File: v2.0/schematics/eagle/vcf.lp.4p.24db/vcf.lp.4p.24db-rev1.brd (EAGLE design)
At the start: 98.7 x 54.6 mm, 97 parts, among them IC1 TL082P, IC2 TL084P, IC3 LM13700N, IC4 LM13700N, IC5 LM13700N, IC6 TL082P, IC7 TL082P, IC8 TL082P, J1 IN, J2 OUT, T1 2N3904, T2 2N3904, T3 2N3904, T4 2N3906, T5 2N3906, T6 2N3906, T7 2N3906

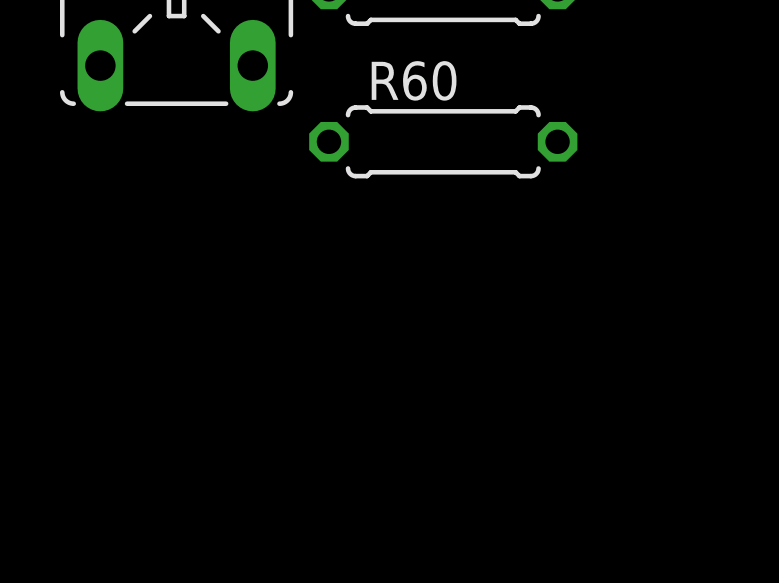
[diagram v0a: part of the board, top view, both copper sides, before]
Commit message: VFC-LP: Upates from schem review
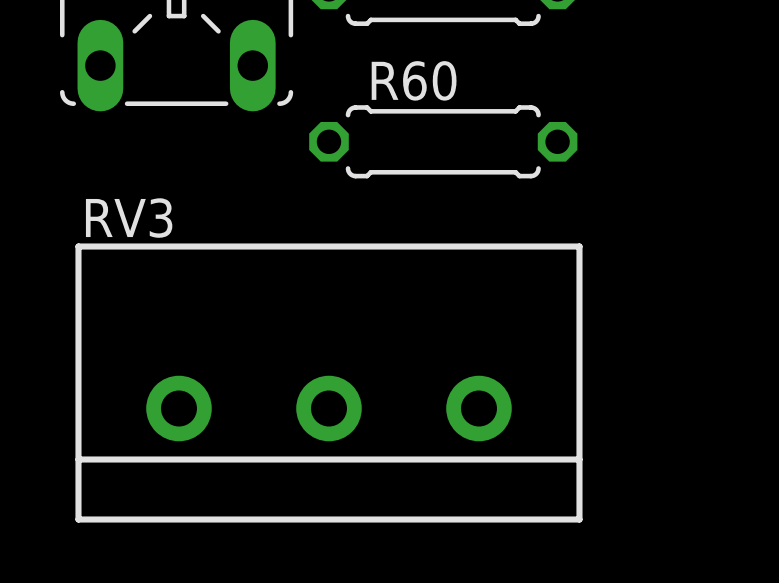
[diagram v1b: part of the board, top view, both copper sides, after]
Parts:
- added RV3: 100K (B), _common:_COMMON_3RP/1610N
- R27, R33: value 39K -> 43K
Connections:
- removed net N$54: R55.E, R57.1
- new net N$62: J1.P$3, RV3.2
- new net N$64: R55.E, R57.1, RV1.2
- net +12V: no longer RV1.2
- net 0V: now also RV3.1
- net N$49: now also RV3.3; no longer J1.P$3
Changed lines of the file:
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@@
 <attribute name="VALUE" x="-51.816" y="-178.3588" size="1.27" layer="27" ratio="10"/>
 </element>
-<element name="R27" library="resistor" package="0207/7" value="39K" x="-49.53" y="-182.88" smashed="yes">
+<element name="R27" library="resistor" package="0207/7" value="43K" x="-49.53" y="-182.88" smashed="yes">
 <attribute name="NAME" x="-52.07" y="-181.483" size="1.27" layer="25" ratio="10"/>
 <attribute name="VALUE" x="-51.816" y="-183.4388" size="1.27" layer="27" ratio="10"/>
@@
 <attribute name="VALUE" x="-51.816" y="-216.4588" size="1.27" layer="27" ratio="10"/>
 </element>
-<element name="R33" library="resistor" package="0207/7" value="39K" x="-49.53" y="-220.98" smashed="yes">
+<element name="R33" library="resistor" package="0207/7" value="43K" x="-49.53" y="-220.98" smashed="yes">
 <attribute name="NAME" x="-52.07" y="-219.583" size="1.27" layer="25" ratio="10"/>
 <attribute name="VALUE" x="-51.816" y="-221.5388" size="1.27" layer="27" ratio="10"/>
@@
 <attribute name="POPULARITY" value="10" x="-58.42" y="-425.45" size="1.778" layer="27" display="off"/>
 <attribute name="VALUE" x="-62.23" y="-430.911" size="1.27" layer="27" ratio="10"/>
+</element>
+<element name="RV3" library="_common" package="_COMMON_3RP/1610N" value="100K (B)" x="-53.34" y="-439.42" smashed="yes">
+<attribute name="NAME" x="-61.595" y="-433.705" size="1.27" layer="25"/>
+<attribute name="VALUE" x="-56.515" y="-436.88" size="1.27" layer="27"/>
 </element>
 </elements>
@@
 <contactref element="R52" pad="1"/>
 <contactref element="R58" pad="1"/>
+<contactref element="RV3" pad="1"/>
 <wire x1="-49.53" y1="-170.18" x2="-53.34" y2="-187.96" width="0" layer="19" extent="1-1"/>
 <wire x1="-49.53" y1="-208.28" x2="-53.34" y2="-187.96" width="0" layer="19" extent="1-1"/>
@@
 <wire x1="91.44" y1="2.54" x2="91.44" y2="6.35" width="0" layer="19" extent="1-1"/>
 <wire x1="-53.34" y1="-420.37" x2="-53.34" y2="-370.84" width="0" layer="19" extent="1-1"/>
+<wire x1="-58.34" y1="-439.42" x2="-53.34" y2="-420.37" width="0" layer="19" extent="1-1"/>
 </signal>
 <signal name="+12V" class="1">
@@
 <contactref element="R29" pad="2"/>
 <contactref element="R35" pad="2"/>
-<contactref element="RV1" pad="2"/>
 <contactref element="R57" pad="2"/>
 <contactref element="R61" pad="E"/>
@@
 <wire x1="68" y1="33.71" x2="43.1" y2="50.8" width="0" layer="19" extent="1-1"/>
 <wire x1="92.71" y1="24.13" x2="86.36" y2="17.78" width="0" layer="19" extent="1-1"/>
-<wire x1="-44.45" y1="-402.59" x2="-45.72" y2="-231.14" width="0" layer="19" extent="1-1"/>
-<wire x1="-45.72" y1="-415.29" x2="-44.45" y2="-402.59" width="0" layer="19" extent="1-1"/>
+<wire x1="-45.72" y1="-415.29" x2="-45.72" y2="-231.14" width="0" layer="19" extent="1-1"/>
 <wire x1="-55.88" y1="-427.99" x2="-45.72" y2="-415.29" width="0" layer="19" extent="1-1"/>
 </signal>
@@
 <wire x1="-52.07" y1="-297.18" x2="-53.34" y2="-304.8" width="0" layer="19" extent="1-1"/>
 </signal>
-<signal name="N$49">
-<contactref element="C13" pad="2"/>
-<contactref element="J1" pad="P$3"/>
-<wire x1="20.32" y1="48.27" x2="-49.53" y2="-297.18" width="0" layer="19" extent="1-1"/>
-</signal>
 <signal name="N$50">
 <contactref element="R45" pad="2"/>
@@
 <wire x1="-53.34" y1="-381" x2="-49.53" y2="-386.08" width="0" layer="19" extent="1-1"/>
 </signal>
-<signal name="N$54">
-<contactref element="R55" pad="E"/>
-<contactref element="R57" pad="1"/>
-<wire x1="-46.99" y1="-391.16" x2="-53.34" y2="-415.29" width="0" layer="19" extent="1-1"/>
-</signal>
 <signal name="N$55">
 <contactref element="IC8" pad="2"/>
@@
 <wire x1="81.28" y1="21.59" x2="-58.42" y2="-422.91" width="0" layer="19" extent="1-1"/>
 </signal>
+<signal name="N$49">
+<contactref element="RV3" pad="3"/>
+<contactref element="C13" pad="2"/>
+<wire x1="-49.53" y1="-297.18" x2="-48.34" y2="-439.42" width="0" layer="19" extent="1-1"/>
+</signal>
+<signal name="N$62">
+<contactref element="J1" pad="P$3"/>
+<contactref element="RV3" pad="2"/>
+<wire x1="20.32" y1="48.27" x2="-53.34" y2="-439.42" width="0" layer="19" extent="1-1"/>
+</signal>
+<signal name="N$64" class="1">
+<contactref element="RV1" pad="2"/>
+<contactref element="R55" pad="E"/>
+<contactref element="R57" pad="1"/>
+<wire x1="-44.45" y1="-402.59" x2="-53.34" y2="-415.29" width="0" layer="19" extent="1-1"/>
+<wire x1="-46.99" y1="-391.16" x2="-44.45" y2="-402.59" width="0" layer="19" extent="1-1"/>
+</signal>
 </signals>

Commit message: VFC-LP: schem renum; power pins; erc approve
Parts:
- added C14, C15, C16, C17, C18, C19, C25: 0.1uF, _common.v1:C025-024X044
- added C20, C21, C22, C23, C24: 100pF, _common.v1:C025-024X044
- C1, C2: value 0.1uF -> 10uF; device _common.v1:C025-024X044 -> _common.v1:E2-5
- C10, C11, C7, C8, C9: value 100pF -> 0.1uF
- C5, C6: value 10uF -> 0.1uF; device _common.v1:E2-5 -> _common.v1:C025-024X044
- IC2: value TL084P -> TL082P; device linear:DIL14 -> linear:DIL08
- IC3, IC5: value LM13700N -> TL082P; device ota:DIL16 -> linear:DIL08
- IC6: value TL082P -> TL084P; device linear:DIL08 -> linear:DIL14
- IC7, IC8: value TL082P -> LM13700N; device linear:DIL08 -> ota:DIL16
- JP1: value (none) -> PWR
- LED1: value (none) -> CV
- R1, R3: value 100K -> 49.9K
- R10: value 100K -> 120K; device pot:CA6V -> resistor:0207/7
- R11: value 27.8K -> 200K
- R12: value 10K -> 470K
- R13: value 1M -> 1.58K
- R14: value 10K -> 1M
- R16: value 100Ω -> 100K
- R17: value 39K -> 10K
- R18: value 20K -> 1M
- R19: value 100K -> 100Ω; device resistor:0207/7 -> pot:CA6V
- R2: value 75K -> 100K; device resistor:0207/7 -> pot:CA6V
- R20: value 39K -> 475Ω
- R21, R28: value 100Ω -> 30K
- R22, R35: value 20K -> 100K
- R24: value 100K -> 27.8K
- R25, R37: value 10K -> 39K
- R26: value 100K -> 1M
- R27: value 43K -> 10K
- R29: value 20K -> 100Ω
- R30: value 10K -> 20K
- R32: value 100K -> 10K
- R33: value 43K -> 150K
- R34: value 100Ω -> 4.7K
- R36: value 100K -> 30K
- R38: value 4.7M -> 100Ω
- R39, R49: value 100K -> 20K
- R4: value 1.58K -> 100K; device resistor:0207/7 -> pot:CA6V
- R42: value 1M -> 10K
- R44: value 30K -> 120K
- R45: value 120K -> 100K
- R46: value 200K -> 30K
- R47: value 1K -> 43K
- R48: value 30K -> 100Ω
- R5: value 10K -> 75K
- R51: value 120K -> 10K
- R52: value 30K -> 100K
- R53: value 100K -> 43K
- R54: value 100K -> 100Ω
- R55: value 100K -> 20K; device pot:CA6V -> resistor:0207/7
- R56: value 49.9K -> 100K
- R57: value 49.9K -> 10K
- R58: value 30K -> 4.7M
- R59: value 4.7K -> 100K
- R6: value 100Ω -> 100K; device pot:CA6V -> resistor:0207/7
- R60: value 150K -> 100K
- R61: value 100K -> 1K; device pot:CA6V -> resistor:0207/7
- R7: value 475Ω -> 100K
- R8: value 470K -> 100K
- R9: value 1M -> 100K; device resistor:0207/7 -> pot:CA6V
- moved R9 470.9 mm to (-58.4, -425.4), turned to 0 degrees
- moved R10 416.6 mm to (-49.5, -365.8)
- moved R1 407.5 mm to (-49.5, -415.3)
- moved C7 394.9 mm to (-59.7, -447.0)
- moved R3 392.4 mm to (-49.5, -410.2)
- moved IC1 381.9 mm to (-45.7, -346.7)
- moved R2 376.1 mm to (-49.5, -388.6)
- moved R6 362.1 mm to (-49.5, -381.0)
- moved C8 348.1 mm to (-59.7, -454.7)
- moved IC6 320.3 mm to (19.1, 30.5), turned to 90 degrees
- moved C9 292.2 mm to (-59.7, -462.3)
- moved IC8 265.5 mm to (-40.6, -81.3)
- moved R11 264.3 mm to (-49.5, -304.8)
- moved C10 261.8 mm to (-59.7, -469.9)
- moved R16 256.5 mm to (-49.5, -375.9)
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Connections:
- new net N$54: R1.1, R2.E, RV1.2
- net +12V: now also C1.+, C11.1, C13.1, C15.1, C17.1, C5.1, C7.1, C9.1, IC2.8, IC3.8, IC5.8, IC6.4, R1.2, R17.2, R26.2, R30.2, R39.2, R4.E, R49.2, R55.2, R9.E; no longer C1.1, C5.+, IC2.4, R10.E, R13.2, R18.2, R22.2, R29.2, R35.2, R5.2, R57.2, R61.E
- net -12V: now also C10.2, C12.2, C14.2, C16.2, C18.2, C2.-, C6.2, C8.2, IC2.4, IC3.4, IC5.4, IC6.11, R16.1, R25.1, R3.1, R34.1, R37.1, R47.1, R5.1, R9.A; no longer C2.2, C6.-, IC2.11, R17.1, R2.1, R20.1, R27.1, R33.1, R56.1, R59.1, R61.A
- net 0V: now also C1.-, C10.1, C12.1, C13.2, C14.1, C15.2, C16.1, C17.2, C18.1, C2.+, C21.2, C22.2, C23.2, C24.2, C5.2, C6.1, C7.2, C8.1, IC2.3, IC2.5, IC4.13, IC4.4, IC5.3, IC5.5, IC7.14, IC8.14, R20.1, R29.1, R36.1, R41.1, R48.1, R54.1, R59.1; no longer C1.2, C10.2, C2.1, C5.-, C6.+, C8.2, IC1.5, IC3.14, IC4.3, IC5.4, IC6.3, R16.1, R28.1, R34.1, R39.1, R47.1, R52.1, R7.1
- net N$1: now also R4.A, R5.2; no longer R10.A, R2.2
- net N$10: now also R24.1; no longer R11.1
- net N$11: now also C20.1, IC2.7, R24.2, R27.1; no longer C7.1, IC1.7, R11.2, R12.1
- net N$12: now also C20.2, IC2.6, R26.1; no longer C7.2, IC1.6, R13.1
- net N$13: now also R19.A, R20.2; no longer R6.A, R7.2
- net N$15: now also IC7.1, R42.2; no longer IC3.1, R25.2
- net N$16: now also R32.1; no longer R14.1
- net N$17: now also C21.1, IC6.5, IC7.12; no longer C8.1, IC2.5, IC3.12
- net N$18: now also IC7.16, R32.2; no longer IC3.16, R14.2
- net N$19: now also IC7.15, R30.1; no longer IC3.15, R18.1
- net N$2: now also R4.S, R8.1; no longer R1.1, R10.S
- net N$20: now also IC7.4, R35.2, R37.2, R38.2, R40.1; no longer IC3.4, R19.2, R20.2, R21.2, R23.1
- net N$21: now also IC7.2, R39.1; no longer IC3.2, R22.1
- net N$22: now also IC7.13, R23.2, R25.2, R29.2, R31.1, R33.1; no longer IC3.13, R15.1, R16.2, R17.2, R24.2, R60.1
- net N$23: now also R42.1; no longer R25.1
- net N$24: now also C22.1, IC6.10, IC7.5; no longer C9.1, IC2.10, IC3.5
- net N$25: now also IC6.8, IC6.9, R40.2, R45.1; no longer IC2.8, IC2.9, R23.2, R26.1
- net N$26: now also IC8.13, R45.2, R47.2, R48.2, R50.1; no longer IC4.13, R26.2, R27.2, R28.2, R31.1
- net N$27: now also IC8.4, R52.2, R53.2, R54.2, R56.1; no longer IC4.4, R32.2, R33.2, R34.2, R36.1
- net N$28: now also IC8.15, R49.1; no longer IC4.15, R29.1
- net N$29: now also IC6.13, IC6.14, R50.2, R52.1; no longer IC2.13, IC2.14, R31.2, R32.1
- net N$3: now also R7.1; no longer R3.1
- net N$30: now also C23.1, IC6.12, IC8.12; no longer C10.1, IC2.12, IC4.12
- net N$31: now also IC8.16, R51.2; no longer IC4.16, R30.2
- net N$32: now also R51.1; no longer R30.1
- net N$33: now also IC8.1, R57.2; no longer IC4.1, R37.2
- net N$34: now also IC8.2, R55.1; no longer IC4.2, R35.1
- net N$35: now also R17.1; no longer R5.1
- net N$36: now also R12.1, R14.1; no longer R8.1, R9.1
- net N$38: now also R57.1; no longer R37.1
- net N$39: now also C25.2, IC6.1, IC6.2, R56.2; no longer C12.2, IC2.1, IC2.2, R36.2
- net N$4: now also R19.S; no longer R6.S
- net N$40: now also C25.1, IC3.5, R58.2; no longer C12.1, IC6.5, R38.2
- net N$41: now also C24.1, IC6.3, IC8.5; no longer C11.1, IC2.3, IC4.5
- net N$42: now also IC3.6, R59.2, R60.1; no longer IC6.6, R39.2, R40.1
- net N$43: now also IC3.7, R46.2, R60.2, R61.1; no longer IC6.7, R40.2, R41.1, R44.2
- net N$44: now also R61.2; no longer R41.2
- net N$45: now also IC3.1, R18.2, R23.1; no longer IC6.1, R24.1, R42.2
- net N$46: now also IC3.2, R11.2, R18.1; no longer IC6.2, R42.1, R43.2
- net N$47: now also IC5.1, R43.2, R44.1; no longer IC7.1, R45.1, R46.2
- net N$48: now also C19.1, R11.1; no longer C13.1, R43.1
- net N$49: now also C19.2; no longer C13.2
- net N$5: now also IC2.2, R13.1, R7.2, R8.2; no longer IC1.2, R1.2, R3.2, R4.1
- net N$50: now also IC5.2, R44.2, R46.1; no longer IC7.2, R44.1, R45.2
- net N$51: now also IC4.3, R41.2, R43.1; no longer IC5.3, R46.1, R47.2
- net N$52: now also R2.A, R3.2; no longer R55.A, R56.2
- net N$53: now also R2.S, R6.1; no longer R54.1, R55.S
- net N$55: now also IC1.2, R10.1, R6.2; no longer IC8.2, R51.1, R54.2
- net N$56: now also IC4.5, IC4.7, R36.2; no longer IC5.5, IC5.7, R58.2
- net N$57: now also IC1.1, R10.2, R15.1; no longer IC8.1, R50.1, R51.2
- net N$58: now also IC1.6, R15.2, R22.1; no longer IC8.6, R49.1, R50.2
- net N$59: now also IC4.8, R33.2, R34.2; no longer IC5.8, R59.2, R60.2
- net N$6: now also IC2.1, R13.2, R14.2, R19.E; no longer IC1.1, R4.2, R6.E, R9.2
- net N$60: now also IC1.5, R16.2, R21.2; no longer IC8.5, R52.2, R53.2
- net N$61: now also IC1.7, R22.2, R28.1; no longer IC8.7, R48.1, R49.2
- net N$63: now also IC4.1, R28.2; no longer IC5.1, R48.2
- net N$64: now also IC5.6, IC5.7; no longer R55.E, R57.1, RV1.2
- net N$7: now also IC6.6, IC6.7, R31.2, R35.1; no longer IC2.6, IC2.7, R15.2, R19.1
- net N$8: now also R27.2; no longer R12.2
- net N$9: now also R12.2, R9.S; no longer R61.S, R8.2
- net V+: now also IC4.11, IC7.11, IC8.11; no longer IC6.8, IC7.8, IC8.8
- net V-: now also IC4.6, IC7.6, IC8.6; no longer IC6.4, IC7.4, IC8.4
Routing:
- net +12V: track 107.6 -> 91.4 mm
- net -12V: track 208.0 -> 198.0 mm

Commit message: VCF-LP: Removed CV RES; Updated values from test build
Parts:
- removed LED1: CV, led:LED3MM
- removed R1, R3: 49.9K, resistor:0207/7
- removed R10, R44: 120K, resistor:0207/7
- removed R12: 470K, resistor:0207/7
- removed R14: 1M, resistor:0207/7
- removed R15, R16, R22, R6: 100K, resistor:0207/7
- removed R17: 10K, resistor:0207/7
- removed R2, R9: 100K, pot:CA6V
- removed R21, R28, R36: 30K, resistor:0207/7
- removed R33: 150K, resistor:0207/7
- removed R34: 4.7K, resistor:0207/7
- removed R41: 1K, resistor:0207/7
- removed T1: 2N3904, transistor-neu-to92:TO92-EBC
- added JP3: RES BOOST, pinhead:1X03
- added R62, R63: 100K, resistor:0207/7
- R13: value 1.58K -> 1.5K
- R19: value 100Ω -> 100K; device pot:CA6V -> resistor:0207/7
- R20: value 475Ω -> 470Ω
- R24: value 27.8K -> 27K
- R43: value 200K -> 20K
- R45, R52: value 100K -> 120K
- R46: value 30K -> 10K
- R47, R53: value 43K -> 39K
- R5: value 75K -> 39K
- RV1: value 100K (B) -> 10K (B)
- RV2: value 100K (B) -> 250K (B)
- RV3: value 100K (B) -> 250K (A)
- moved R19 537.2 mm to (-57.1, -556.3)
- moved RV1 162.8 mm to (-53.3, -565.1)
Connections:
- removed net N$35: R17.1, T1.C
- removed net N$36: R12.1, R14.1, T1.B
- removed net N$37: LED1.A, T1.E
- removed net N$49: C19.2, RV3.3
- removed net N$51: IC4.3, R41.2, R43.1
- removed net N$52: R2.A, R3.2, RV1.1
- removed net N$53: R2.S, R6.1, RV1.3
- removed net N$54: R1.1, R2.E, RV1.2
- removed net N$55: IC1.2, R10.1, R6.2
- removed net N$56: IC4.5, IC4.7, R36.2
- removed net N$57: IC1.1, R10.2, R15.1
- removed net N$58: IC1.6, R15.2, R22.1
- removed net N$59: IC4.8, R33.2, R34.2
- removed net N$60: IC1.5, R16.2, R21.2
- removed net N$61: IC1.7, R22.2, R28.1
- removed net N$62: J1.P$3, RV3.2
- removed net N$63: IC4.1, R28.2
- new net N$39: C25.1, IC3.5, JP3.3, R58.2
- new net N$66: IC5.7, R61.1, R63.2
- net +12V: no longer R1.2, R17.2, R9.E
- net -12V: no longer R16.1, R3.1, R34.1, R9.A
- net 0V: no longer IC1.3, IC4.4, LED1.K, R21.1, R36.1, R41.1
- net N$13: now also R7.1, RV3.3; no longer R19.A, R20.2
- net N$2: now also R19.1; no longer R4.S, R8.1
- net N$22: now also R43.1; no longer R33.1
- net N$3: now also RV3.2; no longer R7.1
- net N$4: now also R4.S, R8.1; no longer D1.A, R19.S, T2.B
- net N$40: now also JP3.2, R46.2; no longer C25.1, IC3.5, R58.2
- net N$43: now also JP3.1, R62.1; no longer R46.2, R61.1
- net N$47: now also RV1.1; no longer R44.1
- net N$5: now also R19.2
- net N$50: now also RV1.2, RV1.3; no longer R44.2
- net N$6: now also D1.A, R20.2, T2.B; no longer R14.2, R19.E
- net N$64: now also R62.2, R63.1; no longer IC5.7
- net N$9: now also C19.2, J1.P$3; no longer R12.2, R9.S
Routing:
- net N$6: track 35.0 -> 0.00 mm
- net +12V: track 91.4 -> 59.0 mm
- net N$36: track 10.2 -> 0.00 mm
- net N$37: track 8.15 -> 0.00 mm
- net N$35: track 6.88 -> 0.00 mm

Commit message: VCF-LF: Schem cleanup for removed ICs; update panel
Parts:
- removed C13, C14, C25: 0.1uF, _common.v1:C025-024X044
- removed C22, C23, C24: 100pF, _common.v1:C025-024X044
- removed IC6: TL084P, linear:DIL14
- removed IC7, IC8: LM13700N, ota:DIL16
- removed R45: 120K, resistor:0207/7
- removed R46, R51, R57: 10K, resistor:0207/7
- removed R48, R54: 100Ω, resistor:0207/7
- removed R49: 20K, resistor:0207/7
- removed R50, R56, R59, R62, R63: 100K, resistor:0207/7
- removed R58: 4.7M, resistor:0207/7
- removed T7: 2N3906, transistor-neu-to92:TO92-EBC
- added R1: 100K, pot:CA6V
- added R10, R17, R3: 100K, resistor:0207/7
- added R12, R2: 39K, resistor:0207/7
- added R14: 10K, resistor:0207/7
- added R15, R21: 100Ω, resistor:0207/7
- added R16, R22: 20K, resistor:0207/7
- added R6: 200K, resistor:0207/7
- added R9: 470Ω, resistor:0207/7
- added T1: 2N3904, transistor-neu-to92:TO92-EBC
- C16, C17, C18, C19: value 0.1uF -> 100pF
- C21: value 100pF -> 0.1uF
- IC2, IC3: value TL082P -> TL084P; device linear:DIL08 -> linear:DIL14
- IC5: value TL082P -> LM13700N; device linear:DIL08 -> ota:DIL16
- R11: value 200K -> 27K
- R13: value 1.5K -> 1M
- R18: value 1M -> 10K
- R20: value 470Ω -> 39K
- R24: value 27K -> 10K
- R25: value 39K -> 20K
- R26: value 1M -> 120K
- R35: value 100K -> 100Ω
- R37, R5: value 39K -> 100K
- R38: value 100Ω -> 10K
- R39: value 20K -> 4.7M
- R4: device pot:CA6V -> resistor:0207/7
- R42: value 10K -> 100K
- R43: value 20K -> 100K
- R7: value 100K -> 1.5K
- R8: value 100K -> 1M
- RV1: value 10K (B) -> 250K (B)
- RV2: value 250K (B) -> 250K (A)
- RV3: value 250K (A) -> 10K (B)
- T3: value 2N3904 -> 2N3906
- moved RV1 623.5 mm to (43.1, 50.8), turned to 180 degrees
- moved IC2 602.2 mm to (-50.8, -575.3)
- moved R4 601.3 mm to (-57.1, -556.3)
- moved RV2 499.6 mm to (-53.3, -439.4), turned to 0 degrees
- moved C16 463.1 mm to (-15.2, -54.6)
- moved R19 421.7 mm to (-49.5, -134.6)
- moved C17 416.7 mm to (-50.8, -106.7)
- moved IC1 381.9 mm to (90.2, 10.2)
- moved R42 381.1 mm to (-57.1, -546.1)
- moved C18 360.8 mm to (-50.8, -170.2)
- moved IC3 320.3 mm to (19.1, 30.5), turned to 90 degrees
- moved R8 285.9 mm to (-49.5, -292.1)
- moved R27 272.8 mm to (-49.5, -320.0)
- moved R11 264.3 mm to (-3.81, -44.5)
- moved IC5 229.9 mm to (-40.6, -81.3)
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- renumbered R47 to R28, R52 to R33, R53 to R34, R55 to R36, R60 to R41, R61 to R44
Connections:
- net +12V: now also IC2.4, IC3.4, R1.E, R13.2, R16.2, R22.2, RV1.2; no longer C13.1, C15.1, C17.1, IC2.8, IC3.8, IC5.8, IC6.4, R26.2, R39.2, R4.E, R49.2, RV2.2
- net -12V: now also IC2.11, IC3.11, R12.1, R2.1, R20.1; no longer C14.2, C16.2, C18.2, IC2.4, IC3.4, IC5.4, IC6.11, R25.1, R37.1, R5.1
- net 0V: now also C18.2, C19.2, C20.2, IC1.3, IC1.5, IC2.10, IC4.3, IC5.14, R15.1, R21.1, R35.1, R39.1, R40.1, R9.1, RV2.1, T2.B, T3.E; no longer C13.2, C14.1, C15.2, C16.1, C18.1, C21.2, C22.2, C23.2, C24.2, IC3.3, IC4.13, IC5.5, IC7.14, IC7.3, IC8.14, IC8.3, R20.1, R38.1, R48.1, R54.1, R58.1, R59.1, RV3.1, T3.B, T7.E
- net N$1: now also R1.A, R2.2, RV1.1; no longer R4.A, R5.2, RV2.1
- net N$10: now also R11.1; no longer R24.1
- net N$11: now also C16.1, IC1.7, R11.2, R14.1; no longer C20.1, IC2.7, R24.2, R27.1
- net N$12: now also C16.2, IC1.6, R13.1, T1.C; no longer C20.2, IC2.6, R26.1, T2.C
- net N$13: now also R3.1, RV2.3; no longer R7.1, RV3.3
- net N$14: now also T2.C, T3.B; no longer T3.C, T7.B
- net N$15: now also IC4.1, R24.2; no longer IC7.1, R42.2
- net N$16: now also R18.1, T3.C; no longer R32.1, T4.C
- net N$17: now also C17.1, IC3.5, IC4.12; no longer C21.1, IC6.5, IC7.12
- net N$18: now also IC4.16, R18.2; no longer IC7.16, R32.2
- net N$19: now also IC4.15, R16.1; no longer IC7.15, R30.1
- net N$2: now also R4.1, RV1.3; no longer R19.1, RV2.3
- net N$20: now also IC4.4, R19.2, R20.2, R21.2, R23.1; no longer IC7.4, R35.2, R37.2, R38.2, R40.1
- net N$21: now also IC4.2, R22.1; no longer IC7.2, R39.1
- net N$22: now also IC4.13, R10.2, R12.2, R15.2, R17.1, R25.1; no longer IC7.13, R23.2, R25.2, R29.2, R31.1, R43.1
- net N$23: now also R24.1, T4.C; no longer R42.1, T5.C
- net N$24: now also C18.1, IC3.10, IC4.5; no longer C22.1, IC6.10, IC7.5
- net N$25: now also IC3.8, IC3.9, R23.2, R26.1; no longer IC6.8, IC6.9, R40.2, R45.1
- net N$26: now also IC5.13, R26.2, R29.2, R31.1; no longer IC8.13, R45.2, R48.2, R50.1
- net N$27: now also IC5.4, R35.2, R37.1; no longer IC8.4, R54.2, R56.1
- net N$28: now also IC5.15, R30.1; no longer IC8.15, R49.1
- net N$29: now also IC3.13, IC3.14, R31.2; no longer IC6.13, IC6.14, R50.2
- net N$3: now also RV2.2; no longer RV3.2
- net N$30: now also C19.1, IC3.12, IC5.12; no longer C23.1, IC6.12, IC8.12
- net N$31: now also IC5.16, R32.2; no longer IC8.16, R51.2
- net N$32: now also R32.1, T5.C; no longer R51.1, T6.C
- net N$33: now also IC5.1, R38.2; no longer IC8.1, R57.2
- net N$34: now also IC5.2; no longer IC8.2
- net N$38: now also R38.1, T6.C; no longer R57.1, T7.C
- net N$39: now also C21.1, IC2.12, R39.2; no longer C25.1, IC3.5, R58.2
- net N$4: now also R1.S, R5.1; no longer R4.S, R8.1
- net N$40: now also R27.2; no longer R46.2
- net N$41: now also C20.1, IC3.3, IC5.5; no longer C24.1, IC6.3, IC8.5
- net N$42: now also IC2.13, R40.2; no longer IC3.6, R59.2
- net N$43: now also IC2.14, R42.1; no longer IC3.7, R62.1
- net N$45: now also IC2.1, R10.1, R8.2; no longer IC3.1, R18.2, R23.1
- net N$46: now also IC2.2, R6.2, R8.1; no longer IC3.2, R11.2, R18.1
- net N$47: now also IC2.7, R25.2, RV3.1; no longer IC5.1, R43.2, RV1.1
- net N$48: now also C15.1, R6.1; no longer C19.1, R11.1
- net N$5: now also IC1.2, R3.2, R4.2, R5.2, R7.1; no longer IC2.2, R13.1, R19.2, R7.2, R8.2
- net N$50: now also IC2.6, R27.1, RV3.2, RV3.3; no longer IC5.2, R46.1, RV1.2, RV1.3
- net N$6: now also IC1.1, R7.2, R9.2, T1.B; no longer IC2.1, R13.2, R20.2, T2.B
- net N$64: now also IC2.9, R42.2, R43.1; no longer IC5.6, R62.2, R63.1
- net N$65: now also C21.2, IC3.1, IC3.2, R37.2; no longer C25.2, IC6.1, IC6.2, R56.2
- net N$66: now also IC2.8, R43.2; no longer IC5.7, R63.2
- net N$7: now also IC3.6, IC3.7, R17.2, R19.1; no longer IC6.6, IC6.7, R31.2, R35.1
- net N$8: now also R14.2, T1.E; no longer R27.2, T3.E
- net N$9: now also C15.2; no longer C19.2
- net V+: now also IC5.11; no longer IC7.11, IC8.11
- net V-: now also IC5.6; no longer IC7.6, IC8.6
